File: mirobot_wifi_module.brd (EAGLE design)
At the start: 27.9 x 34 mm, 4 parts

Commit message: Version 1.4 of the mian PCB and 1.1 of the WiFi PCB
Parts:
- JP1: device pinhead:1X04/90 -> Child-Friendly-Parts:2X03
- R1, R2: device rcl:0204/5 -> Child-Friendly-Parts:0204/5
- moved R1 19.7 mm to (6.86, 13.2), turned to 90 degrees
- moved JP1 11.2 mm to (5.08, 4.83), turned to 270 degrees
- moved R2 9.96 mm to (3.05, 13.2), turned to 270 degrees
- moved U$1 8.79 mm to (22.2, 18.8)
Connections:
- new net N$6: JP1.5, U$1.NREADY
- new net N$7: JP1.6, U$1.EXT_RESET
- net N$2: now also JP1.2; no longer JP1.4
- net N$3: now also JP1.4; no longer JP1.3
- net N$5: now also JP1.3; no longer JP1.2
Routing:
- net N$7: track 0.00 -> 40.2 mm, vias 0 -> 1
- net N$6: track 0.00 -> 39.3 mm, vias 0 -> 1
- net N$5: track 21.5 -> 34.3 mm
- net N$1: track 23.7 -> 13.6 mm, vias 1 -> 0
- net N$3: track 25.1 -> 32.9 mm
- net N$4: track 27.2 -> 33.1 mm
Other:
- board size 27.9 x 34 mm -> 36.1 x 28.3 mm
- board text added: "Ben Pirt 2014"
- board text added: "USR WiFi Module Breakout Board v1.1"
- board text removed: "USR WiFi Breakout Board"
- board text removed: "© Ben Pirt 2013"

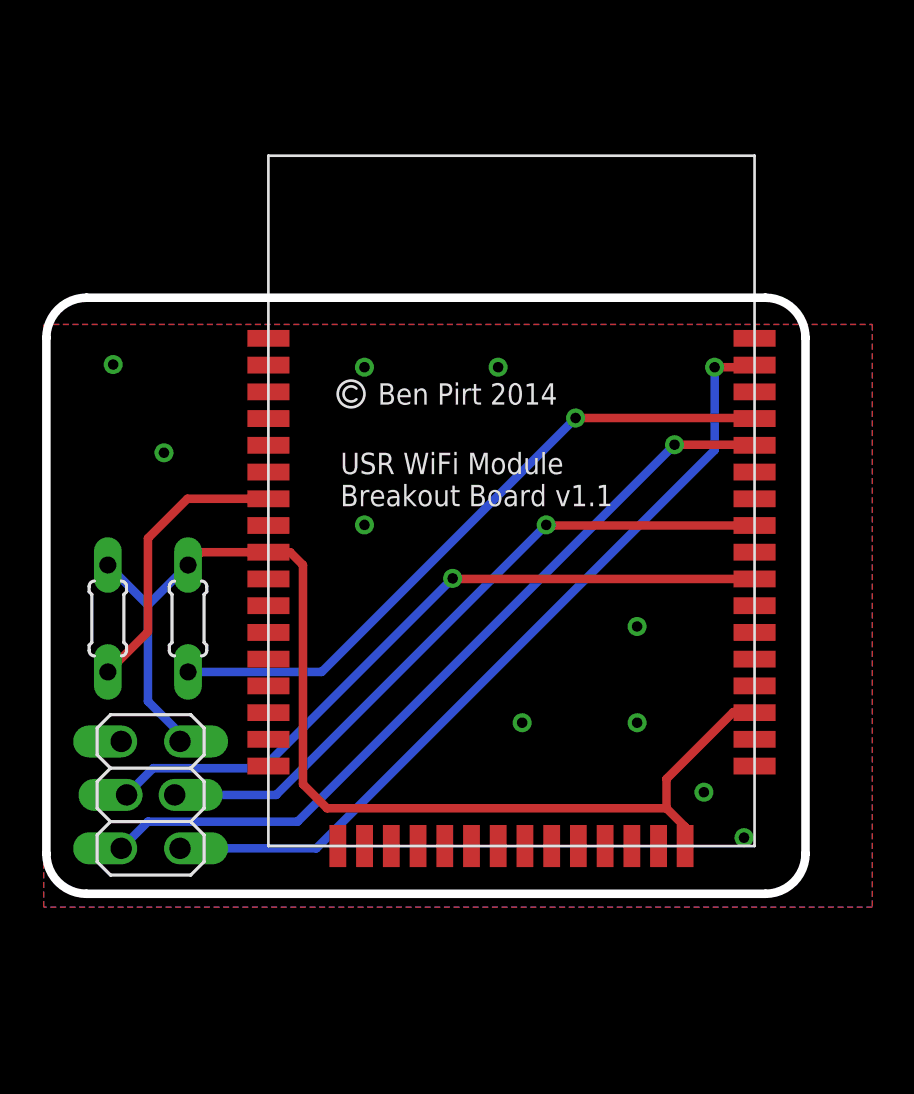
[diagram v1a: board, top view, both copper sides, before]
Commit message: Fix crossed RX and TX lines on the WiFi module
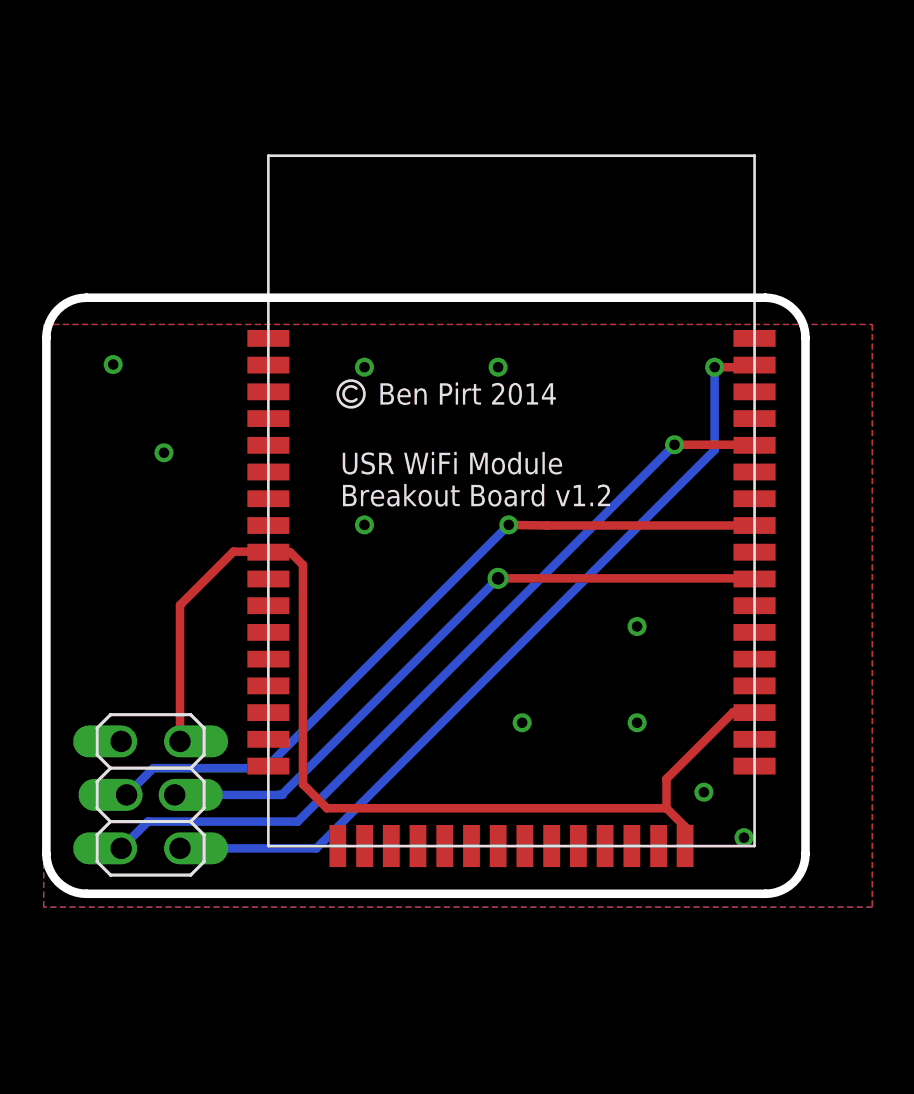
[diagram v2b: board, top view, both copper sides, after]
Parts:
- removed R1: 50K, Child-Friendly-Parts:0204/5
- removed R2: 100K, Child-Friendly-Parts:0204/5
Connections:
- removed net N$1: R2.2, U$1.ALARM1
- removed net N$4: R1.1, U$1.NRELOAD
- net N$2: no longer R1.2, R2.1
- net N$3: now also JP1.3; no longer JP1.4
- net N$5: now also JP1.4; no longer JP1.3
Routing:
- net N$4: track 33.1 -> 0.00 mm, vias 1 -> 0
- net N$1: track 13.6 -> 0.00 mm
- net N$2: track 56.9 -> 52.1 mm
- net N$5: track 34.3 -> 31.9 mm
- net N$3: track 32.9 -> 35.2 mm
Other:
- board text added: "USR WiFi Module Breakout Board v1.2"
- board text removed: "USR WiFi Module Breakout Board v1.1"
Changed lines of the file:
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@@
 <plain>
 <text x="14.097" y="18.542" size="1.016" layer="25">USR WiFi Module
-Breakout Board v1.1</text>
+Breakout Board v1.2</text>
 <text x="15.875" y="23.368" size="1.016" layer="25">Ben Pirt 2014</text>
 <wire x1="36.195" y1="26.543" x2="36.195" y2="2.032" width="0.4064" layer="20"/>
@@
 <elements>
 <element name="U$1" library="usr_wifi" package="WIFI_MODULE" value="USR_WIFI" x="22.225" y="18.796" smashed="yes"/>
-<element name="R1" library="Child-Friendly-Parts" package="0204/5" value="50K" x="6.858" y="13.208" smashed="yes" rot="R90">
-<attribute name="VALUE" x="6.4516" y="14.1986" size="0.6096" layer="27" ratio="10" rot="R270"/>
-</element>
-<element name="R2" library="Child-Friendly-Parts" package="0204/5" value="100K" x="3.048" y="13.208" smashed="yes" rot="R270">
-<attribute name="VALUE" x="2.6416" y="14.3256" size="0.6096" layer="27" ratio="10" rot="R270"/>
-</element>
 <element name="JP1" library="Child-Friendly-Parts" package="2X03" value="" x="5.08" y="4.826" smashed="yes" rot="R270">
 <attribute name="VALUE" x="0.635" y="8.636" size="1.27" layer="27" rot="R270"/>
@@
 <contactref element="U$1" pad="DVDD1"/>
 <contactref element="U$1" pad="DVDD3"/>
-<contactref element="R2" pad="1"/>
-<contactref element="R1" pad="2"/>
 <contactref element="JP1" pad="2"/>
-<wire x1="6.477" y1="7.366" x2="6.477" y2="7.747" width="0.4064" layer="16"/>
-<wire x1="6.477" y1="7.747" x2="4.953" y2="9.271" width="0.4064" layer="16"/>
-<wire x1="4.953" y1="9.271" x2="4.953" y2="13.843" width="0.4064" layer="16"/>
-<wire x1="4.953" y1="13.843" x2="6.858" y2="15.748" width="0.4064" layer="16"/>
-<wire x1="4.953" y1="13.843" x2="3.048" y2="15.748" width="0.4064" layer="16"/>
-<wire x1="6.858" y1="15.748" x2="7.466" y2="16.356" width="0.4064" layer="1"/>
-<wire x1="7.466" y1="16.356" x2="10.675" y2="16.356" width="0.4064" layer="1"/>
 <wire x1="10.675" y1="16.356" x2="11.711" y2="16.356" width="0.4064" layer="1"/>
 <wire x1="11.711" y1="16.356" x2="12.319" y2="15.748" width="0.4064" layer="1"/>
@@
 <wire x1="32.766" y1="8.763" x2="34.383" y2="8.763" width="0.4064" layer="1"/>
 <wire x1="34.383" y1="8.763" x2="33.775" y2="8.736" width="0.4064" layer="1"/>
+<wire x1="6.477" y1="7.366" x2="6.477" y2="13.843" width="0.4064" layer="1"/>
+<wire x1="6.477" y1="13.843" x2="9.017" y2="16.383" width="0.4064" layer="1"/>
+<wire x1="9.017" y1="16.383" x2="10.648" y2="16.383" width="0.4064" layer="1"/>
+<wire x1="10.648" y1="16.383" x2="10.675" y2="16.356" width="0.4064" layer="1"/>
 </signal>
 <signal name="N$3">
 <contactref element="U$1" pad="UART0_RX"/>
-<contactref element="JP1" pad="4"/>
 <wire x1="33.775" y1="17.626" x2="23.903" y2="17.626" width="0.4064" layer="1"/>
-<wire x1="23.903" y1="17.626" x2="23.876" y2="17.653" width="0.4064" layer="1"/>
-<via x="23.876" y="17.653" extent="1-16" drill="0.5"/>
-<wire x1="23.876" y1="17.653" x2="11.049" y2="4.826" width="0.4064" layer="16"/>
-<wire x1="11.049" y1="4.826" x2="6.223" y2="4.826" width="0.4064" layer="16"/>
+<wire x1="23.903" y1="17.626" x2="22.098" y2="17.653" width="0.4064" layer="1"/>
+<via x="22.098" y="17.653" extent="1-16" drill="0.5"/>
+<wire x1="22.098" y1="17.653" x2="10.541" y2="6.096" width="0.4064" layer="16"/>
+<contactref element="JP1" pad="3"/>
+<wire x1="10.541" y1="6.096" x2="5.207" y2="6.096" width="0.4064" layer="16"/>
+<wire x1="5.207" y1="6.096" x2="3.937" y2="4.826" width="0.4064" layer="16"/>
 </signal>
 <signal name="N$5">
 <contactref element="U$1" pad="UART0_TX"/>
-<contactref element="JP1" pad="3"/>
-<wire x1="33.775" y1="15.086" x2="19.331" y2="15.086" width="0.4064" layer="1"/>
-<wire x1="19.331" y1="15.086" x2="19.431" y2="15.113" width="0.4064" layer="1"/>
-<via x="19.431" y="15.113" extent="1-16" drill="0.5"/>
-<wire x1="19.431" y1="15.113" x2="10.414" y2="6.096" width="0.4064" layer="16"/>
-<wire x1="10.414" y1="6.096" x2="5.207" y2="6.096" width="0.4064" layer="16"/>
-<wire x1="5.207" y1="6.096" x2="3.937" y2="4.826" width="0.4064" layer="16"/>
+<contactref element="JP1" pad="4"/>
+<wire x1="11.357" y1="4.826" x2="11.303" y2="4.826" width="0.4064" layer="16"/>
+<wire x1="11.176" y1="4.826" x2="6.223" y2="4.826" width="0.4064" layer="16"/>
+<wire x1="33.775" y1="15.086" x2="33.748" y2="15.113" width="0.4064" layer="1"/>
+<wire x1="33.748" y1="15.113" x2="21.59" y2="15.113" width="0.4064" layer="1"/>
+<via x="21.59" y="15.113" extent="1-16" drill="0.6"/>
+<wire x1="21.59" y1="15.113" x2="11.303" y2="4.826" width="0.4064" layer="16"/>
+<wire x1="11.303" y1="4.826" x2="11.176" y2="4.826" width="0.4064" layer="16"/>
 </signal>
 <signal name="GND">
@@
 <contactref element="U$1" pad="GND2"/>
 <contactref element="U$1" pad="GND1"/>
-<polygon width="0.4064" layer="16">
+<polygon width="0.4064" layer="16" isolate="1.27">
 <vertex x="0" y="27.178"/>
 <vertex x="39.37" y="27.178"/>
@@
 <via x="22.733" y="8.255" extent="1-16" drill="0.5"/>
 </signal>
-<signal name="N$1">
-<contactref element="U$1" pad="ALARM1"/>
-<contactref element="R2" pad="2"/>
-<wire x1="10.675" y1="18.896" x2="6.831" y2="18.896" width="0.4064" layer="1"/>
-<wire x1="6.831" y1="18.896" x2="4.953" y2="17.018" width="0.4064" layer="1"/>
-<wire x1="4.953" y1="17.018" x2="4.953" y2="12.573" width="0.4064" layer="1"/>
-<wire x1="4.953" y1="12.573" x2="3.048" y2="10.668" width="0.4064" layer="1"/>
-</signal>
-<signal name="N$4">
-<contactref element="U$1" pad="NRELOAD"/>
-<contactref element="R1" pad="1"/>
-<wire x1="6.858" y1="10.668" x2="13.208" y2="10.668" width="0.4064" layer="16"/>
-<wire x1="13.208" y1="10.668" x2="25.273" y2="22.733" width="0.4064" layer="16"/>
-<via x="25.273" y="22.733" extent="1-16" drill="0.5"/>
-<wire x1="25.273" y1="22.733" x2="34.383" y2="22.733" width="0.4064" layer="1"/>
-<wire x1="34.383" y1="22.733" x2="33.775" y2="22.706" width="0.4064" layer="1"/>
-</signal>
 <signal name="N$6">
